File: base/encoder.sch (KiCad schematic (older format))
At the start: 0 parts

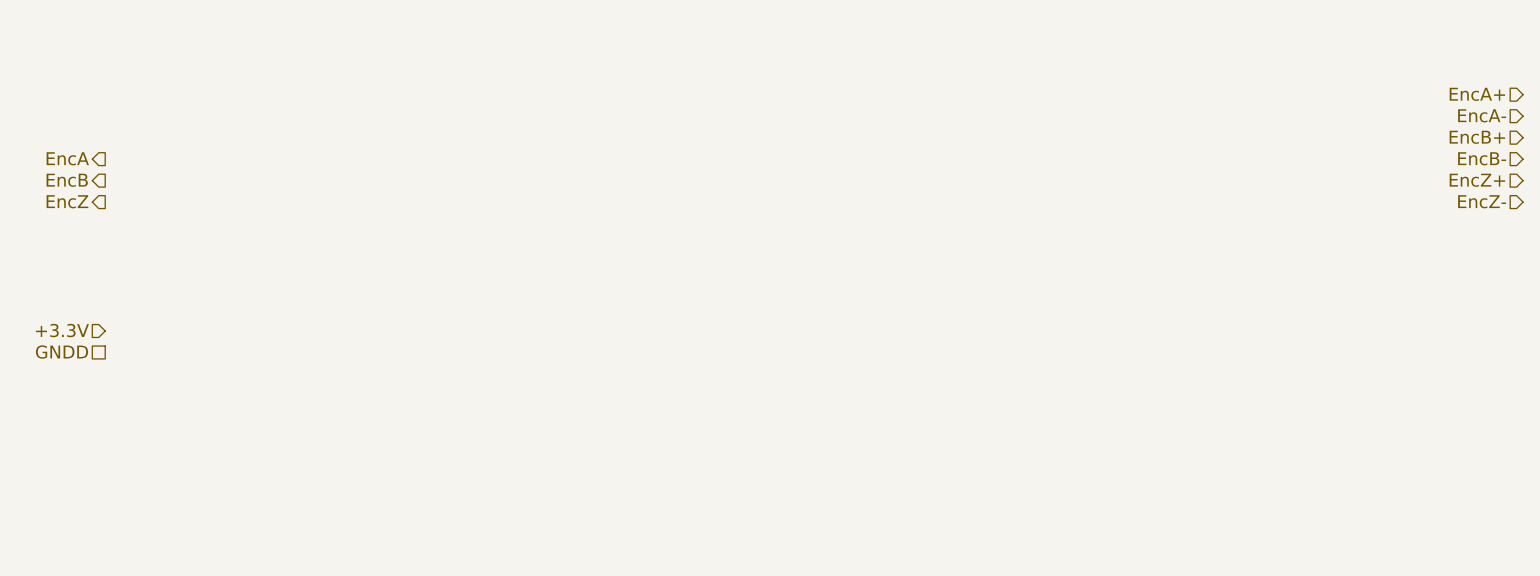
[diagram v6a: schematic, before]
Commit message: encoder.sch was modified
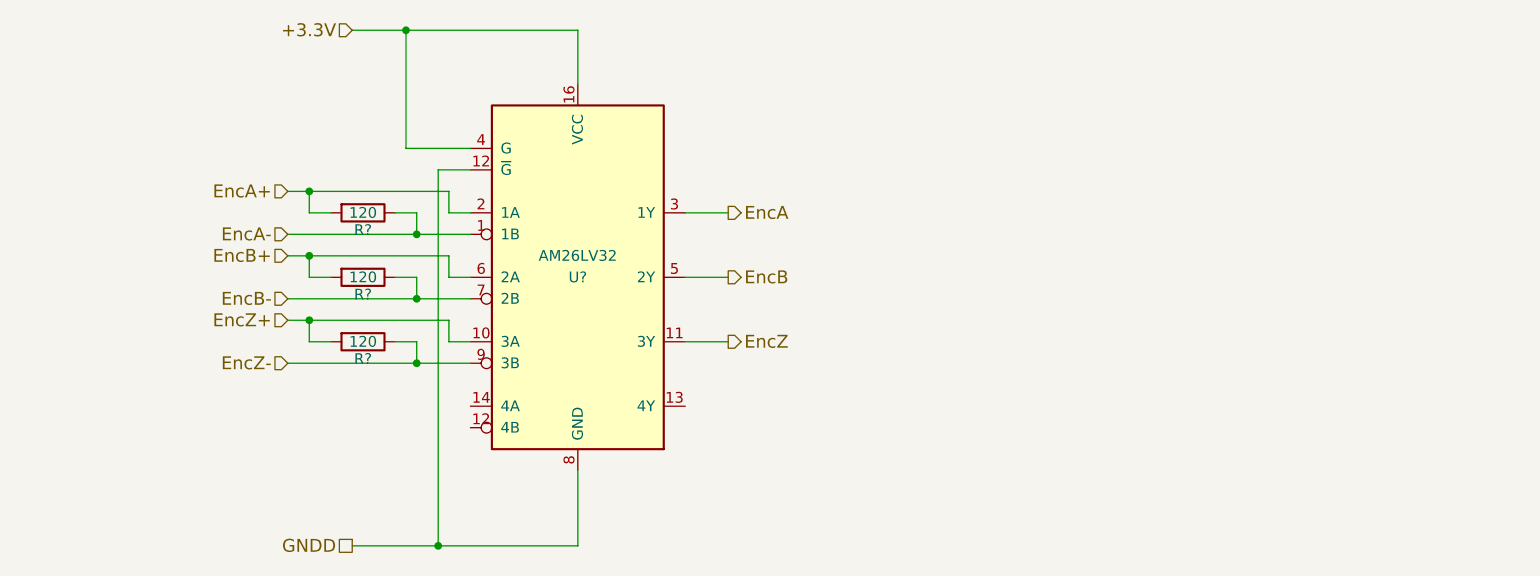
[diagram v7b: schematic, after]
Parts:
- added R? (x3): 120, symbol R
- added U?: AM26LV32, Housings_SOIC:SOIC-16_3.9x9.9mm_Pitch1.27mm, symbol AM26LV32
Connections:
- net +3.3V: now also U?.16 (VCC), U?.4 (G)
- net EncA: now also U?.3 (1Y)
- net EncA+: now also R?.2, U?.2 (1A)
- net EncA-: now also R?.1, U?.1 (1B)
- net EncB: now also U?.5 (2Y)
- net EncB+: now also R?.2, U?.6 (2A)
- net EncB-: now also R?.1, U?.7 (2B)
- net EncZ: now also U?.11 (3Y)
- net EncZ+: now also R?.2, U?.10 (3A)
- net EncZ-: now also R?.1, U?.9 (3B)
- net GNDD: now also U?.12 (~G), U?.8 (GND)
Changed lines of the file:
@@
 LIBS:interface
 LIBS:ESD_Protection
+LIBS:texas
 LIBS:4hbd-base-cache
 EELAYER 25 0
@@
 Comment4 ""
 $EndDescr
-Text HLabel 2600 2700 0    60   Output ~ 0
+Text HLabel 5500 2950 2    60   Output ~ 0
 EncA
-Text HLabel 2600 2800 0    60   Output ~ 0
+Text HLabel 5500 3250 2    60   Output ~ 0
 EncB
-Text HLabel 2600 2900 0    60   Output ~ 0
+Text HLabel 5500 3550 2    60   Output ~ 0
 EncZ
-Text HLabel 9200 2400 0    60   Input ~ 0
+Text HLabel 3450 2850 0    60   Input ~ 0
 EncA+
-Text HLabel 9200 2500 0    60   Input ~ 0
+Text HLabel 3450 3050 0    60   Input ~ 0
 EncA-
-Text HLabel 9200 2600 0    60   Input ~ 0
+Text HLabel 3450 3150 0    60   Input ~ 0
 EncB+
-Text HLabel 9200 2700 0    60   Input ~ 0
+Text HLabel 3450 3350 0    60   Input ~ 0
 EncB-
-Text HLabel 9200 2800 0    60   Input ~ 0
+Text HLabel 3450 3450 0    60   Input ~ 0
 EncZ+
-Text HLabel 9200 2900 0    60   Input ~ 0
+Text HLabel 3450 3650 0    60   Input ~ 0
 EncZ-
-Text HLabel 2600 3500 0    60   Input ~ 0
+Text HLabel 3750 2100 0    60   Input ~ 0
 +3.3V
-Text HLabel 2600 3600 0    60   UnSpc ~ 0
+Text HLabel 3750 4500 0    60   UnSpc ~ 0
 GNDD
+$Comp
+L AM26LV32 U?
+U 1 1 5A42515F
+P 4800 3250
+F 0 "U?" H 4800 3250 50  0000 C CNN
+F 1 "AM26LV32" H 4800 3350 50  0000 C CNN
+F 2 "Housings_SOIC:SOIC-16_3.9x9.9mm_Pitch1.27mm" H 4900 2300 50  0001 C CNN
+F 3 "" H 4800 3250 50  0001 C CNN
+	1    4800 3250
+	1    0    0    -1
+$EndComp
+Wire Wire Line
+	3750 2100 4800 2100
+Wire Wire Line
+	4800 2100 4800 2350
+Wire Wire Line
+	4300 2650 4000 2650
+Wire Wire Line
+	4000 2650 4000 2100
+Connection ~ 4000 2100
+Wire Wire Line
+	3750 4500 4800 4500
+Wire Wire Line
+	4800 4500 4800 4150
+Wire Wire Line
+	4300 2750 4150 2750
+Wire Wire Line
+	4150 2750 4150 4500
+Connection ~ 4150 4500
+$Comp
+L R R?
+U 1 1 5A425215
+P 3800 2950
+F 0 "R?" V 3880 2950 50  0000 C CNN
+F 1 "120" V 3800 2950 50  0000 C CNN
+F 2 "" V 3730 2950 50  0001 C CNN
+F 3 "" H 3800 2950 50  0001 C CNN
+	1    3800 2950
+	0    1    1    0
+$EndComp
+Wire Wire Line
+	3450 2850 4200 2850
+Wire Wire Line
+	4200 2850 4200 2950
+Wire Wire Line
+	4200 2950 4300 2950
+Wire Wire Line
+	3450 3050 4300 3050
+Wire Wire Line
+	3550 2850 3550 2950
+Connection ~ 3550 2850
+Wire Wire Line
+	3450 3150 4200 3150
+Wire Wire Line
+	4200 3150 4200 3250
+Wire Wire Line
+	4200 3250 4300 3250
+Wire Wire Line
+	3450 3350 4300 3350
+$Comp
+L R R?
+U 1 1 5A425315
+P 3800 3250
+F 0 "R?" V 3880 3250 50  0000 C CNN
+F 1 "120" V 3800 3250 50  0000 C CNN
+F 2 "" V 3730 3250 50  0001 C CNN
+F 3 "" H 3800 3250 50  0001 C CNN
+	1    3800 3250
+	0    1    1    0
+$EndComp
+Wire Wire Line
+	3650 3250 3550 3250
+Wire Wire Line
+	3550 3250 3550 3150
+Connection ~ 3550 3150
+Wire Wire Line
+	3950 3250 4050 3250
+Wire Wire Line
+	4050 3250 4050 3350
+Connection ~ 4050 3350
+Wire Wire Line
+	3950 2950 4050 2950
+Wire Wire Line
+	3550 2950 3650 2950
+Wire Wire Line
+	4050 2950 4050 3050
+Connection ~ 4050 3050
+Wire Wire Line
+	4300 3650 3450 3650
+$Comp
+L R R?
+U 1 1 5A425470
+P 3800 3550
+F 0 "R?" V 3880 3550 50  0000 C CNN
+F 1 "120" V 3800 3550 50  0000 C CNN
+F 2 "" V 3730 3550 50  0001 C CNN
+F 3 "" H 3800 3550 50  0001 C CNN
+	1    3800 3550
+	0    1    1    0
+$EndComp
+Wire Wire Line
+	3450 3450 4200 3450
+Wire Wire Line
+	4200 3450 4200 3550
+Wire Wire Line
+	4200 3550 4300 3550
+Wire Wire Line
+	3950 3550 4050 3550
+Wire Wire Line
+	4050 3550 4050 3650
+Connection ~ 4050 3650
+Wire Wire Line
+	3650 3550 3550 3550
+Wire Wire Line
+	3550 3550 3550 3450
+Connection ~ 3550 3450
+Wire Wire Line
+	5300 2950 5500 2950
+Wire Wire Line
+	5300 3250 5500 3250
+Wire Wire Line
+	5300 3550 5500 3550
 $EndSCHEMATC
